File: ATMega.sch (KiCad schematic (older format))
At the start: 23 parts

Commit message: fix footprints
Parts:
- R? (x2): footprint (none) -> Resistor_SMD:R_0603_1608Metric
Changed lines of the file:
@@
 F 0 "R?" V 4600 5200 50  0000 C CNN
 F 1 "10k" H 4659 5155 50  0001 L CNN
-F 2 "" H 4600 5200 50  0001 C CNN
+F 2 "Resistor_SMD:R_0603_1608Metric" H 4600 5200 50  0001 C CNN
 F 3 "~" H 4600 5200 50  0001 C CNN
 	1    4600 5200
@@
 F 0 "R?" V 4700 5200 50  0000 C CNN
 F 1 "10k" H 4750 5200 50  0000 L CNN
-F 2 "" H 4700 5200 50  0001 C CNN
+F 2 "Resistor_SMD:R_0603_1608Metric" H 4700 5200 50  0001 C CNN
 F 3 "~" H 4700 5200 50  0001 C CNN
 	1    4700 5200

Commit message: annotate parts
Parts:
- gave numbers to parts that had none: 23
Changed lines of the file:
@@
 $EndDescr
 $Comp
-L MCU_Microchip_ATmega:ATmega2560-16AU U?
+L MCU_Microchip_ATmega:ATmega2560-16AU U1
 U 1 1 5C280BF8
 P 3450 3950
-F 0 "U?" H 2850 1150 50  0000 C CNN
+F 0 "U1" H 2850 1150 50  0000 C CNN
 F 1 "ATmega2560-16AU" H 2850 1050 50  0000 C CNN
 F 2 "Package_QFP:TQFP-100_14x14mm_P0.5mm" H 3450 3950 50  0001 C CIN
@@
 	3450 1000 3450 950
 $Comp
-L power:GND #PWR?
+L power:GND #PWR07
 U 1 1 5C280F6E
 P 3450 6950
-F 0 "#PWR?" H 3450 6700 50  0001 C CNN
+F 0 "#PWR07" H 3450 6700 50  0001 C CNN
 F 1 "GND" H 3455 6777 50  0000 C CNN
 F 2 "" H 3450 6950 50  0001 C CNN
@@
 	3450 6850 3450 6950
 $Comp
-L Device:Crystal_Small Y?
+L Device:Crystal_Small Y1
 U 1 1 5C2812F8
 P 2450 1650
-F 0 "Y?" V 2496 1562 50  0000 R CNN
+F 0 "Y1" V 2496 1562 50  0000 R CNN
 F 1 "16MHz" V 2405 1562 50  0000 R CNN
 F 2 "Crystal:Crystal_SMD_5032-2Pin_5.0x3.2mm" H 2450 1650 50  0001 C CNN
@@
 	2450 1750 2650 1750
 $Comp
-L Device:C_Small C?
+L Device:C_Small C2
 U 1 1 5C2814DA
 P 2250 1550
-F 0 "C?" V 2021 1550 50  0000 C CNN
+F 0 "C2" V 2021 1550 50  0000 C CNN
 F 1 "8pF" V 2112 1550 50  0000 C CNN
 F 2 "Capacitor_SMD:C_0603_1608Metric" H 2250 1550 50  0001 C CNN
@@
 $EndComp
 $Comp
-L Device:C_Small C?
+L Device:C_Small C3
 U 1 1 5C281519
 P 2250 1750
-F 0 "C?" V 2450 1750 50  0000 C CNN
+F 0 "C3" V 2450 1750 50  0000 C CNN
 F 1 "8pF" V 2350 1750 50  0000 C CNN
 F 2 "Capacitor_SMD:C_0603_1608Metric" H 2250 1750 50  0001 C CNN
@@
 	2100 1750 2150 1750
 $Comp
-L power:GND #PWR?
+L power:GND #PWR06
 U 1 1 5C28167C
 P 2100 1850
-F 0 "#PWR?" H 2100 1600 50  0001 C CNN
+F 0 "#PWR06" H 2100 1600 50  0001 C CNN
 F 1 "GND" H 2105 1677 50  0000 C CNN
 F 2 "" H 2100 1850 50  0001 C CNN
@@
 Connection ~ 2100 1750
 $Comp
-L Device:R R?
+L Device:R R3
 U 1 1 5C281CF1
 P 2400 2250
-F 0 "R?" V 2400 2250 50  0000 C CNN
+F 0 "R3" V 2400 2250 50  0000 C CNN
 F 1 "5.6" V 2450 2450 50  0000 C CNN
 F 2 "Resistor_SMD:R_0603_1608Metric" V 2330 2250 50  0001 C CNN
@@
 $EndComp
 $Comp
-L Device:R R?
+L Device:R R4
 U 1 1 5C281E2C
 P 2400 2350
-F 0 "R?" V 2400 2350 50  0000 C CNN
+F 0 "R4" V 2400 2350 50  0000 C CNN
 F 1 "5.6" V 2450 2550 50  0000 C CNN
 F 2 "Resistor_SMD:R_0603_1608Metric" V 2330 2350 50  0001 C CNN
@@
 $EndComp
 $Comp
-L Device:R R?
+L Device:R R5
 U 1 1 5C281E58
 P 2400 2450
-F 0 "R?" V 2400 2450 50  0000 C CNN
+F 0 "R5" V 2400 2450 50  0000 C CNN
 F 1 "5.6" V 2450 2650 50  0000 C CNN
 F 2 "Resistor_SMD:R_0603_1608Metric" V 2330 2450 50  0001 C CNN
@@
 $EndComp
 $Comp
-L Device:R R?
+L Device:R R6
 U 1 1 5C281E76
 P 2400 2550
-F 0 "R?" V 2400 2550 50  0000 C CNN
+F 0 "R6" V 2400 2550 50  0000 C CNN
 F 1 "5.6" V 2450 2750 50  0000 C CNN
 F 2 "Resistor_SMD:R_0603_1608Metric" V 2330 2550 50  0001 C CNN
@@
 	2550 2550 2650 2550
 $Comp
-L Device:LED_Small D?
+L Device:LED_Small D1
 U 1 1 5C2825A8
 P 2100 2250
-F 0 "D?" H 2200 2200 50  0000 C CNN
+F 0 "D1" H 2200 2200 50  0000 C CNN
 F 1 " " H 1750 2350 50  0000 C CNN
 F 2 "LED_SMD:LED_0603_1608Metric" V 2100 2250 50  0001 C CNN
@@
 $EndComp
 $Comp
-L Device:LED_Small D?
+L Device:LED_Small D2
 U 1 1 5C2825D4
 P 2100 2350
-F 0 "D?" H 2200 2300 50  0000 C CNN
+F 0 "D2" H 2200 2300 50  0000 C CNN
 F 1 " " H 2100 2494 50  0000 C CNN
 F 2 "LED_SMD:LED_0603_1608Metric" V 2100 2350 50  0001 C CNN
@@
 $EndComp
 $Comp
-L Device:LED_Small D?
+L Device:LED_Small D3
 U 1 1 5C2825F8
 P 2100 2450
-F 0 "D?" H 2200 2400 50  0000 C CNN
+F 0 "D3" H 2200 2400 50  0000 C CNN
 F 1 " " H 2100 2594 50  0000 C CNN
 F 2 "LED_SMD:LED_0603_1608Metric" V 2100 2450 50  0001 C CNN
@@
 $EndComp
 $Comp
-L Device:LED_Small D?
+L Device:LED_Small D4
 U 1 1 5C282622
 P 2100 2550
-F 0 "D?" H 2200 2500 50  0000 C CNN
+F 0 "D4" H 2200 2500 50  0000 C CNN
 F 1 " " H 2100 2694 50  0000 C CNN
 F 2 "LED_SMD:LED_0603_1608Metric" V 2100 2550 50  0001 C CNN
@@
 	2200 2550 2250 2550
 $Comp
-L power:GND #PWR?
+L power:GND #PWR05
 U 1 1 5C284E11
 P 1950 2600
-F 0 "#PWR?" H 1950 2350 50  0001 C CNN
+F 0 "#PWR05" H 1950 2350 50  0001 C CNN
 F 1 "GND" H 1955 2427 50  0000 C CNN
 F 2 "" H 1950 2600 50  0001 C CNN
@@
 	1950 2550 1950 2450
 $Comp
-L Device:R R?
+L Device:R R7
 U 1 1 5C28BE77
 P 2550 1100
-F 0 "R?" V 2550 1100 50  0000 C CNN
+F 0 "R7" V 2550 1100 50  0000 C CNN
 F 1 "10k" H 2620 1055 50  0000 L CNN
 F 2 "Resistor_SMD:R_0603_1608Metric" V 2480 1100 50  0001 C CNN
@@
 	2600 1950 2650 1950
 $Comp
-L Device:C_Small C?
+L Device:C_Small C4
 U 1 1 5C28F5ED
 P 5350 1400
-F 0 "C?" H 5258 1354 50  0000 R CNN
+F 0 "C4" H 5258 1354 50  0000 R CNN
 F 1 "100nF" H 5258 1445 50  0000 R CNN
 F 2 "Capacitor_SMD:C_0603_1608Metric" H 5350 1400 50  0001 C CNN
@@
 $EndComp
 $Comp
-L Device:C_Small C?
+L Device:C_Small C5
 U 1 1 5C28FBD2
 P 5750 1400
-F 0 "C?" H 5658 1354 50  0000 R CNN
+F 0 "C5" H 5658 1354 50  0000 R CNN
 F 1 "100nF" H 5658 1445 50  0000 R CNN
 F 2 "Capacitor_SMD:C_0603_1608Metric" H 5750 1400 50  0001 C CNN
@@
 $EndComp
 $Comp
-L Device:C_Small C?
+L Device:C_Small C6
 U 1 1 5C28FC1A
 P 6150 1400
-F 0 "C?" H 6058 1354 50  0000 R CNN
+F 0 "C6" H 6058 1354 50  0000 R CNN
 F 1 "100nF" H 6058 1445 50  0000 R CNN
 F 2 "Capacitor_SMD:C_0603_1608Metric" H 6150 1400 50  0001 C CNN
@@
 $EndComp
 $Comp
-L Device:C_Small C?
+L Device:C_Small C7
 U 1 1 5C28FC66
 P 6550 1400
-F 0 "C?" H 6458 1354 50  0000 R CNN
+F 0 "C7" H 6458 1354 50  0000 R CNN
 F 1 "100nF" H 6458 1445 50  0000 R CNN
 F 2 "Capacitor_SMD:C_0603_1608Metric" H 6550 1400 50  0001 C CNN
@@
 $EndComp
 $Comp
-L Device:C_Small C?
+L Device:C_Small C8
 U 1 1 5C28FCBA
 P 6950 1400
-F 0 "C?" H 6858 1354 50  0000 R CNN
+F 0 "C8" H 6858 1354 50  0000 R CNN
 F 1 "100nF" H 6858 1445 50  0000 R CNN
 F 2 "Capacitor_SMD:C_0603_1608Metric" H 6950 1400 50  0001 C CNN
@@
 	5750 1250 6150 1250
 $Comp
-L power:GND #PWR?
+L power:GND #PWR08
 U 1 1 5C29743D
 P 6150 1600
-F 0 "#PWR?" H 6150 1350 50  0001 C CNN
+F 0 "#PWR08" H 6150 1350 50  0001 C CNN
 F 1 "GND" H 6155 1427 50  0000 C CNN
 F 2 "" H 6150 1600 50  0001 C CNN
@@
 	6150 1250 6150 1200
 $Comp
-L Connector_Generic:Conn_02x03_Odd_Even J?
+L Connector_Generic:Conn_02x03_Odd_Even J1
 U 1 1 5C29DEFC
 P 8450 2450
-F 0 "J?" H 8500 2767 50  0000 C CNN
+F 0 "J1" H 8500 2767 50  0000 C CNN
 F 1 "Conn_02x03_Odd_Even" H 8500 2676 50  0000 C CNN
 F 2 "Connector_PinHeader_2.54mm:PinHeader_2x03_P2.54mm_Vertical" H 8450 2450 50  0001 C CNN
@@
 MOSI
 $Comp
-L power:GND #PWR?
+L power:GND #PWR09
 U 1 1 5C2A1657
 P 8800 2650
-F 0 "#PWR?" H 8800 2400 50  0001 C CNN
+F 0 "#PWR09" H 8800 2400 50  0001 C CNN
 F 1 "GND" H 8805 2477 50  0000 C CNN
 F 2 "" H 8800 2650 50  0001 C CNN
@@
 	4350 4150 4550 4150
 $Comp
-L Device:R R?
+L Device:R R8
 U 1 1 5C325691
 P 4350 3850
-F 0 "R?" V 4350 3850 50  0000 C CNN
+F 0 "R8" V 4350 3850 50  0000 C CNN
 F 1 "10k" H 4420 3805 50  0001 L CNN
 F 2 "Resistor_SMD:R_0603_1608Metric" V 4280 3850 50  0001 C CNN
@@
 $EndComp
 $Comp
-L Device:R R?
+L Device:R R9
 U 1 1 5C325799
 P 4500 3850
-F 0 "R?" V 4500 3850 50  0000 C CNN
+F 0 "R9" V 4500 3850 50  0000 C CNN
 F 1 "10k" H 4570 3805 50  0000 L CNN
 F 2 "Resistor_SMD:R_0603_1608Metric" V 4430 3850 50  0001 C CNN
@@
 3V3IN
 $Comp
-L Device:R_Small R?
+L Device:R_Small R10
 U 1 1 5C32D2D3
 P 4600 5200
-F 0 "R?" V 4600 5200 50  0000 C CNN
+F 0 "R10" V 4600 5200 50  0000 C CNN
 F 1 "10k" H 4659 5155 50  0001 L CNN
 F 2 "Resistor_SMD:R_0603_1608Metric" H 4600 5200 50  0001 C CNN
@@
 $EndComp
 $Comp
-L Device:R_Small R?
+L Device:R_Small R11
 U 1 1 5C32D353
 P 4700 5200
-F 0 "R?" V 4700 5200 50  0000 C CNN
+F 0 "R11" V 4700 5200 50  0000 C CNN
 F 1 "10k" H 4750 5200 50  0000 L CNN
 F 2 "Resistor_SMD:R_0603_1608Metric" H 4700 5200 50  0001 C CNN

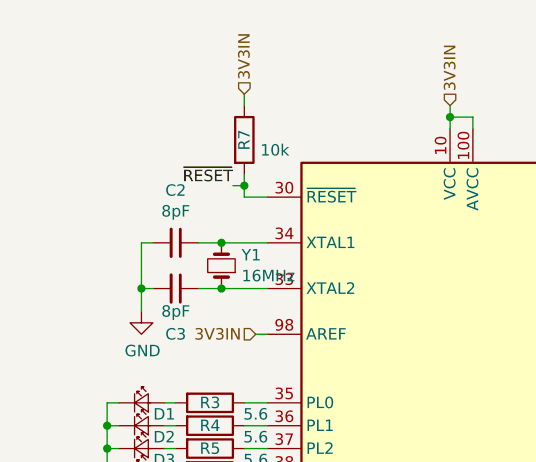
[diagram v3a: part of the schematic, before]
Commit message: add reset switch
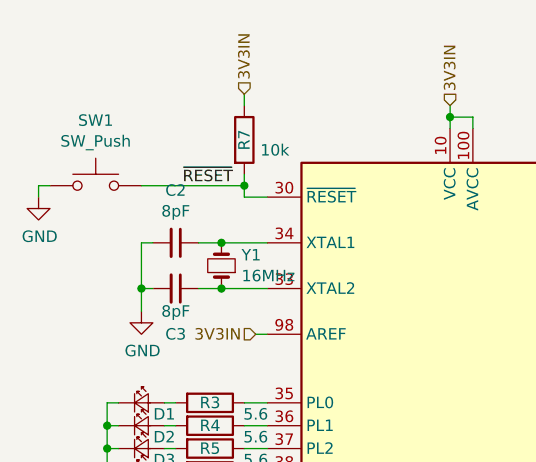
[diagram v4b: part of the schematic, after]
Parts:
- added SW1: SW_Push, Button_Switch_SMD:SW_SPST_PTS810, symbol Switch:SW_Push
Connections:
- net GND: now also SW1.1
- net ~RESET~: now also SW1.2
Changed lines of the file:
@@
 Text Label 2500 1300 2    50   ~ 0
 ~RESET~
-Wire Wire Line
-	2500 1300 2550 1300
 Connection ~ 2550 1300
 Wire Wire Line
@@
 NoConn ~ 4250 6450
 NoConn ~ 4250 6550
+Wire Wire Line
+	2100 1300 2550 1300
+$Comp
+L Switch:SW_Push SW1
+U 1 1 5CA91E69
+P 1900 1300
+F 0 "SW1" H 1900 1585 50  0000 C CNN
+F 1 "SW_Push" H 1900 1494 50  0000 C CNN
+F 2 "Button_Switch_SMD:SW_SPST_PTS810" H 1900 1500 50  0001 C CNN
+F 3 "~" H 1900 1500 50  0001 C CNN
+	1    1900 1300
+	1    0    0    -1
+$EndComp
+Wire Wire Line
+	1700 1300 1650 1300
+Wire Wire Line
+	1650 1300 1650 1350
+$Comp
+L power:GND #PWR0104
+U 1 1 5CA944A5
+P 1650 1350
+F 0 "#PWR0104" H 1650 1100 50  0001 C CNN
+F 1 "GND" H 1655 1177 50  0000 C CNN
+F 2 "" H 1650 1350 50  0001 C CNN
+F 3 "" H 1650 1350 50  0001 C CNN
+	1    1650 1350
+	1    0    0    -1
+$EndComp
 $EndSCHEMATC

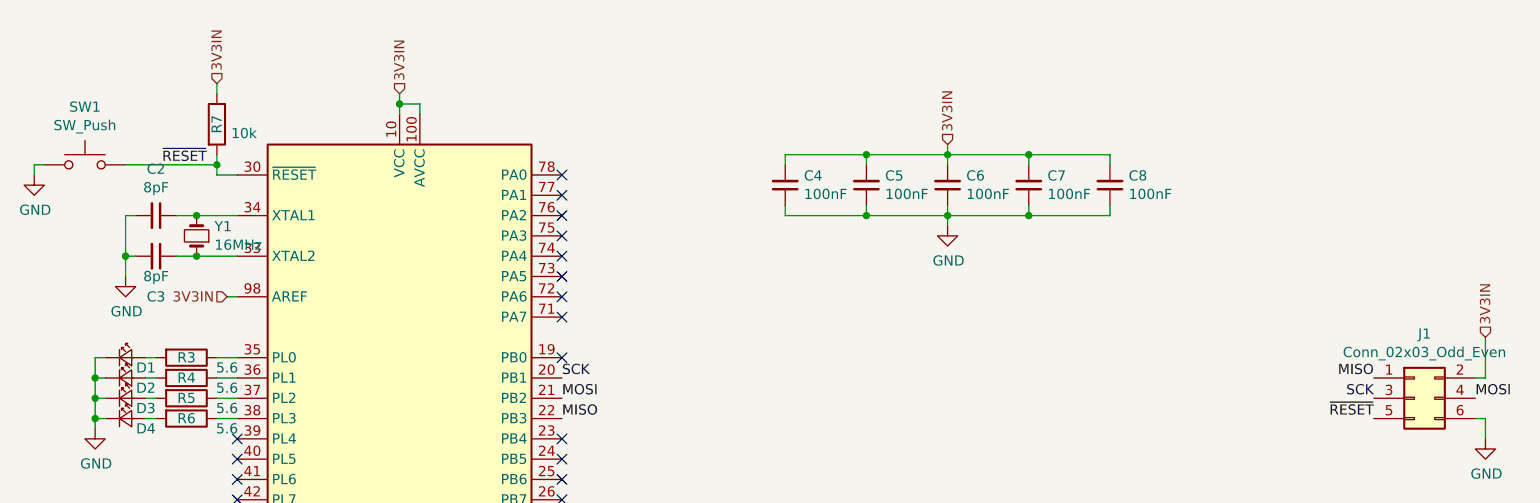
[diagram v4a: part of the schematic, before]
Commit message: LMZM23600 from kicad libs
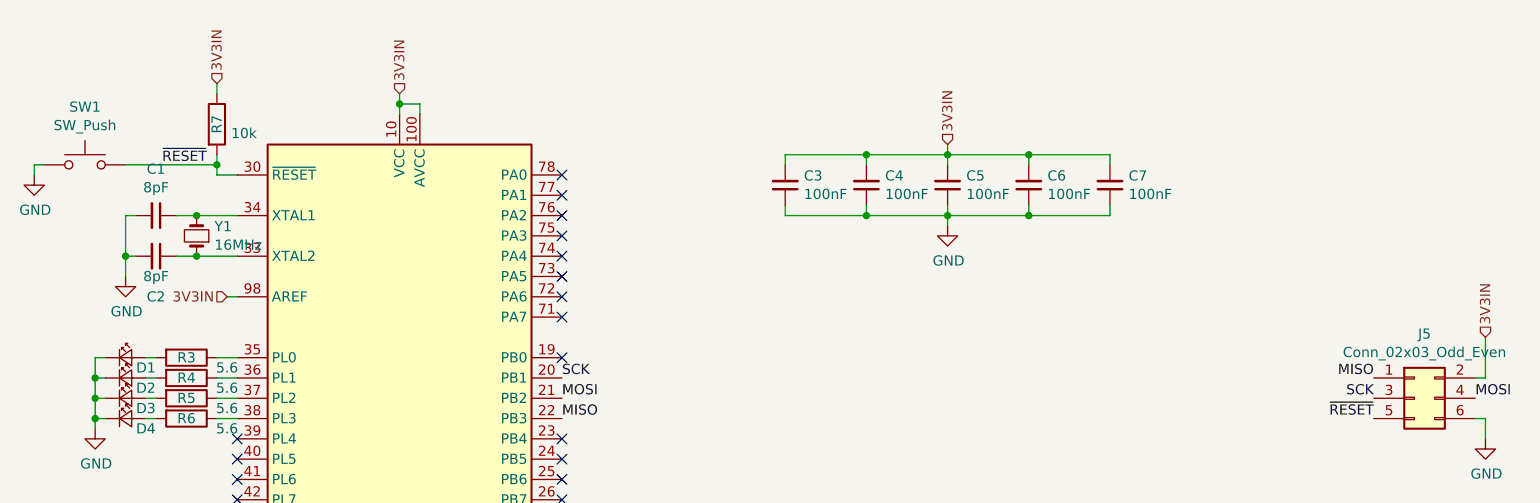
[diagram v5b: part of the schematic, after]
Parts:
- renumbered C2 to C1, C3 to C2, C4 to C3, C5 to C4, C6 to C5, C7 to C6, C8 to C7, J1 to J5
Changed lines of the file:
@@
 	3450 1000 3450 950
 $Comp
-L power:GND #PWR07
+L power:GND #PWR014
 U 1 1 5C280F6E
 P 3450 6950
-F 0 "#PWR07" H 3450 6700 50  0001 C CNN
+F 0 "#PWR014" H 3450 6700 50  0001 C CNN
 F 1 "GND" H 3455 6777 50  0000 C CNN
 F 2 "" H 3450 6950 50  0001 C CNN
@@
 	2450 1750 2650 1750
 $Comp
-L Device:C_Small C2
+L Device:C_Small C1
 U 1 1 5C2814DA
 P 2250 1550
-F 0 "C2" V 2021 1550 50  0000 C CNN
+F 0 "C1" V 2021 1550 50  0000 C CNN
 F 1 "8pF" V 2112 1550 50  0000 C CNN
 F 2 "Capacitor_SMD:C_0603_1608Metric" H 2250 1550 50  0001 C CNN
@@
 $EndComp
 $Comp
-L Device:C_Small C3
+L Device:C_Small C2
 U 1 1 5C281519
 P 2250 1750
-F 0 "C3" V 2450 1750 50  0000 C CNN
+F 0 "C2" V 2450 1750 50  0000 C CNN
 F 1 "8pF" V 2350 1750 50  0000 C CNN
 F 2 "Capacitor_SMD:C_0603_1608Metric" H 2250 1750 50  0001 C CNN
@@
 	2100 1750 2150 1750
 $Comp
-L power:GND #PWR06
+L power:GND #PWR013
 U 1 1 5C28167C
 P 2100 1850
-F 0 "#PWR06" H 2100 1600 50  0001 C CNN
+F 0 "#PWR013" H 2100 1600 50  0001 C CNN
 F 1 "GND" H 2105 1677 50  0000 C CNN
 F 2 "" H 2100 1850 50  0001 C CNN
@@
 	2200 2550 2250 2550
 $Comp
-L power:GND #PWR05
+L power:GND #PWR012
 U 1 1 5C284E11
 P 1950 2600
-F 0 "#PWR05" H 1950 2350 50  0001 C CNN
+F 0 "#PWR012" H 1950 2350 50  0001 C CNN
 F 1 "GND" H 1955 2427 50  0000 C CNN
 F 2 "" H 1950 2600 50  0001 C CNN
@@
 	2600 1950 2650 1950
 $Comp
-L Device:C_Small C4
+L Device:C_Small C3
 U 1 1 5C28F5ED
 P 5350 1400
-F 0 "C4" H 5258 1354 50  0000 R CNN
+F 0 "C3" H 5258 1354 50  0000 R CNN
 F 1 "100nF" H 5258 1445 50  0000 R CNN
 F 2 "Capacitor_SMD:C_0603_1608Metric" H 5350 1400 50  0001 C CNN
@@
 $EndComp
 $Comp
-L Device:C_Small C5
+L Device:C_Small C4
 U 1 1 5C28FBD2
 P 5750 1400
-F 0 "C5" H 5658 1354 50  0000 R CNN
+F 0 "C4" H 5658 1354 50  0000 R CNN
 F 1 "100nF" H 5658 1445 50  0000 R CNN
 F 2 "Capacitor_SMD:C_0603_1608Metric" H 5750 1400 50  0001 C CNN
@@
 $EndComp
 $Comp
-L Device:C_Small C6
+L Device:C_Small C5
 U 1 1 5C28FC1A
 P 6150 1400
-F 0 "C6" H 6058 1354 50  0000 R CNN
+F 0 "C5" H 6058 1354 50  0000 R CNN
 F 1 "100nF" H 6058 1445 50  0000 R CNN
 F 2 "Capacitor_SMD:C_0603_1608Metric" H 6150 1400 50  0001 C CNN
@@
 $EndComp
 $Comp
-L Device:C_Small C7
+L Device:C_Small C6
 U 1 1 5C28FC66
 P 6550 1400
-F 0 "C7" H 6458 1354 50  0000 R CNN
+F 0 "C6" H 6458 1354 50  0000 R CNN
 F 1 "100nF" H 6458 1445 50  0000 R CNN
 F 2 "Capacitor_SMD:C_0603_1608Metric" H 6550 1400 50  0001 C CNN
@@
 $EndComp
 $Comp
-L Device:C_Small C8
+L Device:C_Small C7
 U 1 1 5C28FCBA
 P 6950 1400
-F 0 "C8" H 6858 1354 50  0000 R CNN
+F 0 "C7" H 6858 1354 50  0000 R CNN
 F 1 "100nF" H 6858 1445 50  0000 R CNN
 F 2 "Capacitor_SMD:C_0603_1608Metric" H 6950 1400 50  0001 C CNN
@@
 	5750 1250 6150 1250
 $Comp
-L power:GND #PWR08
+L power:GND #PWR015
 U 1 1 5C29743D
 P 6150 1600
-F 0 "#PWR08" H 6150 1350 50  0001 C CNN
+F 0 "#PWR015" H 6150 1350 50  0001 C CNN
 F 1 "GND" H 6155 1427 50  0000 C CNN
 F 2 "" H 6150 1600 50  0001 C CNN
@@
 	6150 1250 6150 1200
 $Comp
-L Connector_Generic:Conn_02x03_Odd_Even J1
+L Connector_Generic:Conn_02x03_Odd_Even J5
 U 1 1 5C29DEFC
 P 8450 2450
-F 0 "J1" H 8500 2767 50  0000 C CNN
+F 0 "J5" H 8500 2767 50  0000 C CNN
 F 1 "Conn_02x03_Odd_Even" H 8500 2676 50  0000 C CNN
 F 2 "Connector_PinHeader_2.54mm:PinHeader_2x03_P2.54mm_Vertical" H 8450 2450 50  0001 C CNN
@@
 MOSI
 $Comp
-L power:GND #PWR09
+L power:GND #PWR016
 U 1 1 5C2A1657
 P 8800 2650
-F 0 "#PWR09" H 8800 2400 50  0001 C CNN
+F 0 "#PWR016" H 8800 2400 50  0001 C CNN
 F 1 "GND" H 8805 2477 50  0000 C CNN
 F 2 "" H 8800 2650 50  0001 C CNN
@@
 	1650 1300 1650 1350
 $Comp
-L power:GND #PWR0104
+L power:GND #PWR011
 U 1 1 5CA944A5
 P 1650 1350
-F 0 "#PWR0104" H 1650 1100 50  0001 C CNN
+F 0 "#PWR011" H 1650 1100 50  0001 C CNN
 F 1 "GND" H 1655 1177 50  0000 C CNN
 F 2 "" H 1650 1350 50  0001 C CNN
